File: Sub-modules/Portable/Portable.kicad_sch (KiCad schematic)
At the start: 10 parts, among them J2 PR5L5015-5P-C-H, J3 PR5L5015-5P-C-H, U1 STM32U5G9VJTxQ, U10 AT24CS02-SSHM, U4 TLV75733PDBV

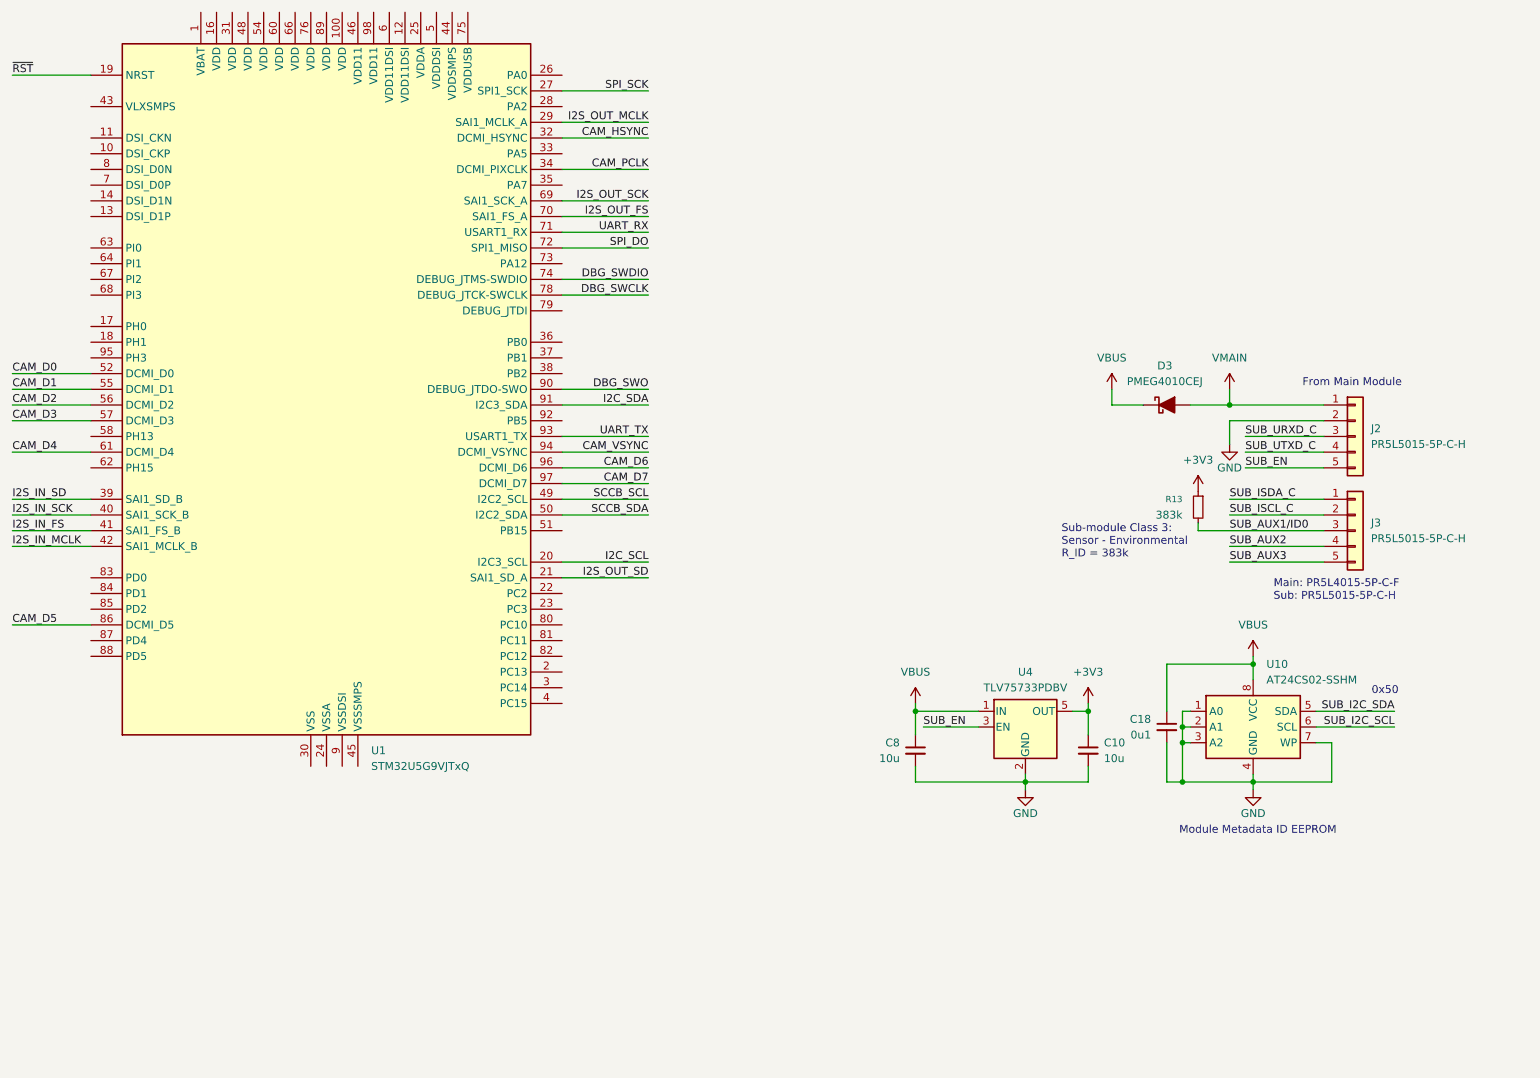
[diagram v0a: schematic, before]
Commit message: Setup STM32U5 pinout for Portable submodule
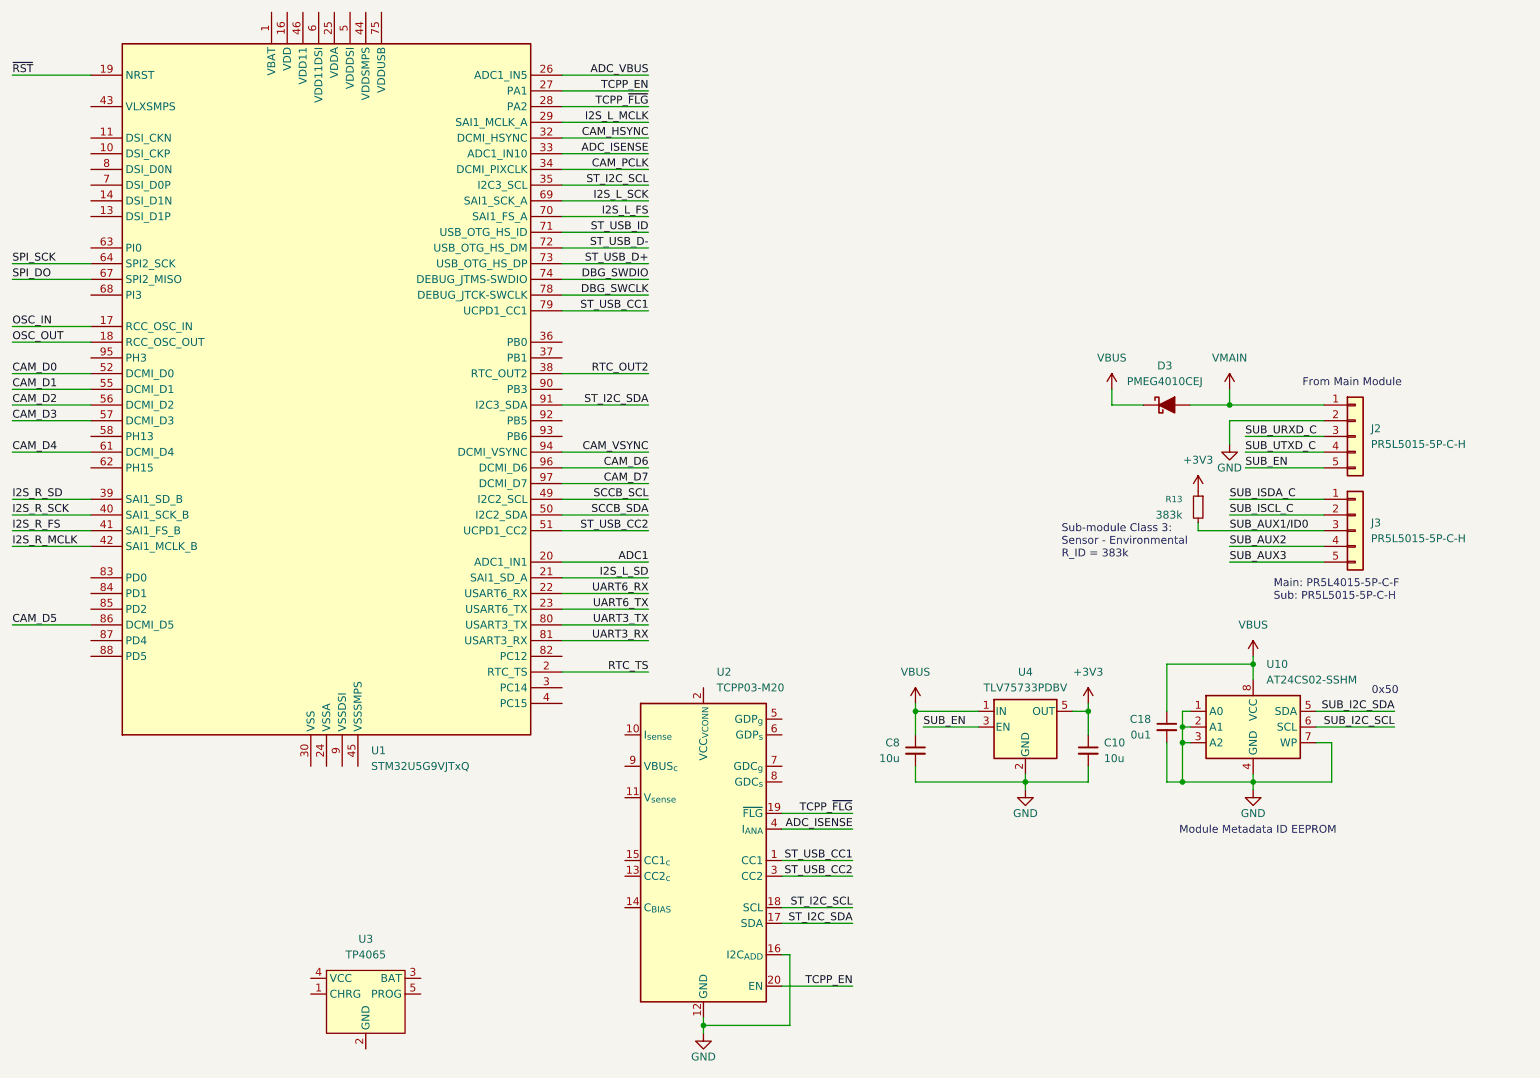
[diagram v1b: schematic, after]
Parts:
- added U2: TCPP03-M20, Package_DFN_QFN:TQFN-20-1EP_4x4mm_P0.5mm_EP2.1x2.1mm, symbol Interface_USB:TCPP03-M20
- added U3: TP4065, Package_TO_SOT_SMD:SOT-23-5_HandSoldering, symbol ESP-HI-PLUS Library:TP4065
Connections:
- net GND: now also U2.12 (GND), U2.16 (I2C_{ADD}), U2.21 (GND)
- net SPI_DO: now also U1.67 (PI2); no longer U1.72 (PA11)
- net SPI_SCK: now also U1.64 (PI1); no longer U1.27 (PA1)
- net VDD: now reaches U1.100 (VDD)
- net VDD: now also U1.16 (VDD), U1.31 (VDD), U1.48 (VDD), U1.54 (VDD), U1.60 (VDD), U1.66 (VDD), U1.76 (VDD), U1.89 (VDD)
- net VDD11DSI: now reaches U1.12 (VDD11DSI)
- net VDD11DSI: now also U1.6 (VDD11DSI)
- net OSC_IN: now reaches U1.17 (PH0)
- net OSC_OUT: now reaches U1.18 (PH1)
- net RTC_TS: now reaches U1.2 (PC13)
- net UART6_RX: now reaches U1.22 (PC2)
- net UART6_TX: now reaches U1.23 (PC3)
- net ADC_VBUS: now reaches U1.26 (PA0)
- net TCPP_~{FLG}: now reaches U1.28 (PA2)
- net TCPP_~{FLG}: now also U2.19 (~{FLG})
- net ADC_ISENSE: now reaches U1.33 (PA5)
- net ADC_ISENSE: now also U2.4 (I_{ANA})
- net ST_I2C_SCL: now reaches U1.35 (PA7)
- net ST_I2C_SCL: now also U2.18 (SCL)
- net RTC_OUT2: now reaches U1.38 (PB2)
- net VDD11: now reaches U1.46 (VDD11)
- net VDD11: now also U1.98 (VDD11)
- net ST_USB_CC2: now reaches U1.51 (PB15)
- net ST_USB_CC2: now also U2.3 (CC2)
- net ST_USB_D+: now reaches U1.73 (PA12)
- net ST_USB_CC1: now reaches U1.79 (PA15)
- net ST_USB_CC1: now also U2.1 (CC1)
- net UART3_TX: now reaches U1.80 (PC10)
- net UART3_RX: now reaches U1.81 (PC11)
- net DBG_SWO: no longer names the net of U1.90 (PB3)
- net I2C_SCL renamed ADC1
- net I2C_SDA renamed ST_I2C_SDA
- net ST_I2C_SDA: now also U2.17 (SDA)
- net I2S_IN_FS renamed I2S_R_FS
- net I2S_IN_MCLK renamed I2S_R_MCLK
- net I2S_IN_SCK renamed I2S_R_SCK
- net I2S_IN_SD renamed I2S_R_SD
- net I2S_OUT_FS renamed I2S_L_FS
- net I2S_OUT_MCLK renamed I2S_L_MCLK
- net I2S_OUT_SCK renamed I2S_L_SCK
- net I2S_OUT_SD renamed I2S_L_SD
- net UART_RX renamed ST_USB_ID
- net UART_TX: no longer names the net of U1.93 (PB6)
- new net ST_USB_D-: U1.72 (PA11)
- new net TCPP_EN: U1.27 (PA1), U2.20 (EN)

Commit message: updated Portable
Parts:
- added D1: WS2812B-2020, LED_SMD:LED_WS2812B-2020_PLCC4_2.0x2.0mm, symbol LED:WS2812B-2020
- R13: value 383k -> 226k
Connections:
- net +3V3: now also D1.4 (VDD)
- net GND: now also D1.2 (VSS)
- net SUB_EN: now also U1.37 (PB1); no longer U4.3 (EN)
- net VBUS: now also U4.3 (EN)
- net LED_DATA: now reaches U1.36 (PB0)
- net LED_DATA: now also D1.3 (DIN)
- no-connect marks 0 -> 1
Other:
- note added: "Sub-module Class 5: Audio - Speaker R_ID = 226k"
- note removed: "Sub-module Class 3: Sensor - Environmental R_ID = 383k"
- moved on the sheet: C10, C18, C8, U10, U4
